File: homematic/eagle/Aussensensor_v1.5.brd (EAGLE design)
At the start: 56.2 x 29.4 mm, 44 parts, among them IC1 Atmega 328P, IC2 MAX1724, IC3 MAX44009, IC4 TSL256FN, IC5 BMP180, IC6 BME280, IC7 DS18B20, M1 CC1101_WIRELES_MODULE, T1 IRML6344

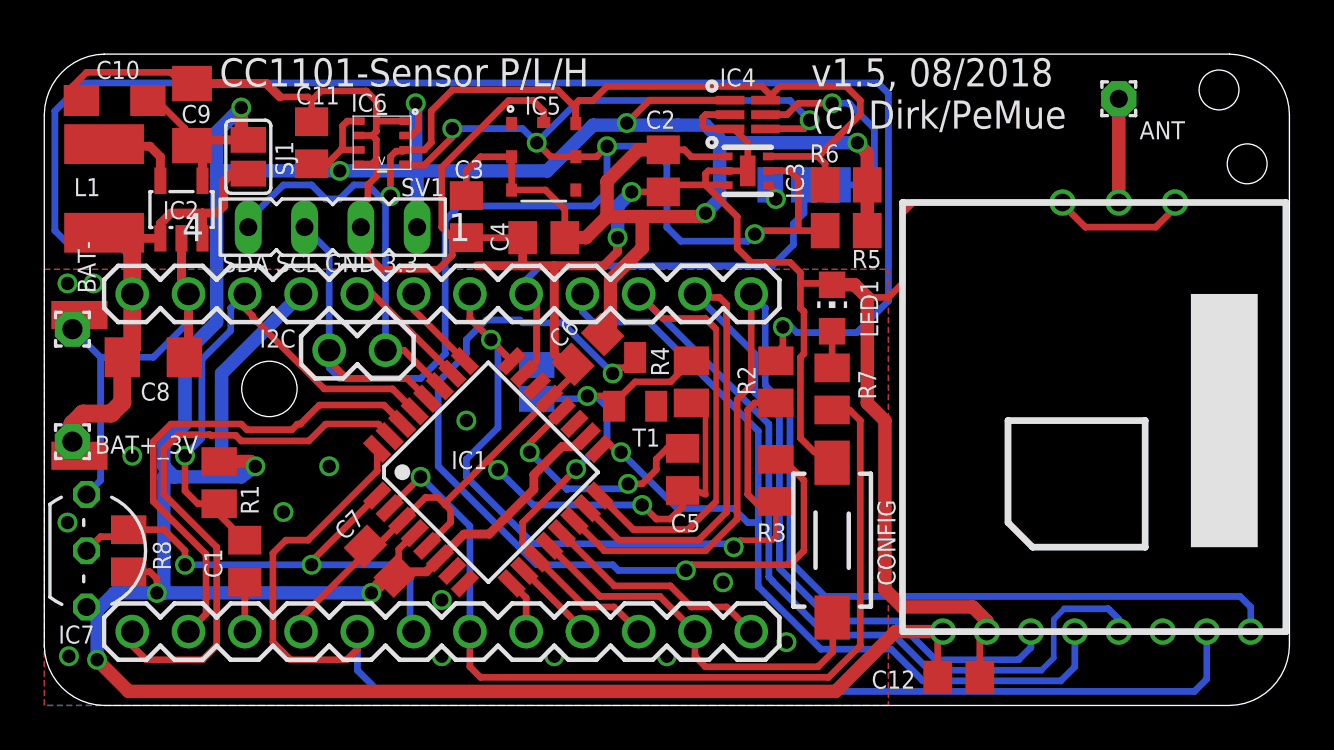
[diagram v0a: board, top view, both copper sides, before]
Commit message: - changes requested by Tom Major
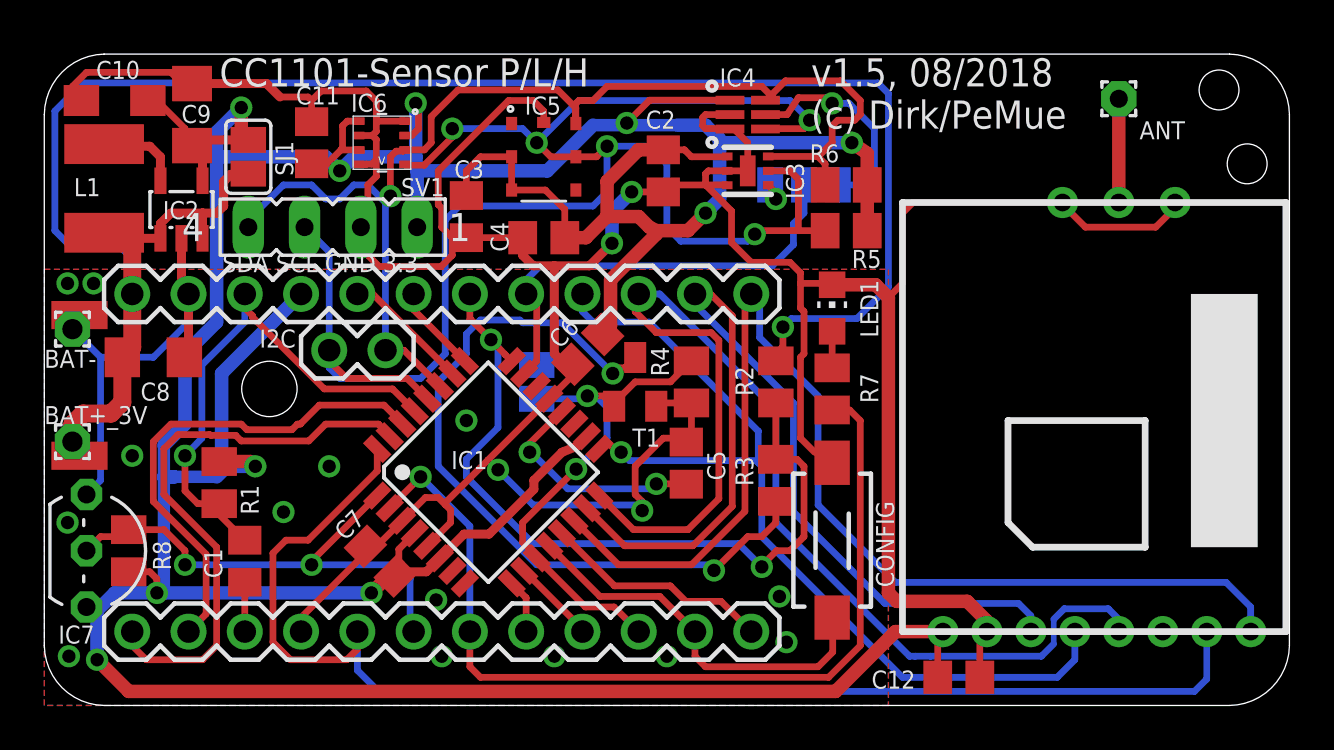
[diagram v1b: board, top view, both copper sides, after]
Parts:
- moved C5 0.33 mm to (29.0, 10.9), turned to 270 degrees
- turned R3 to 270 degrees
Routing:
- net GND: track 193.9 -> 189.1 mm
- net N$3: track 41.1 -> 36.9 mm
- net SCK: track 44.7 -> 41.8 mm
- net MOSI: track 46.4 -> 43.7 mm
- net D10: track 54.5 -> 52.8 mm
- net MISO: track 54.0 -> 52.6 mm
- net A1: track 34.6 -> 35.6 mm
- net U-BAT: track 88.2 -> 87.6 mm
- net +3.3V: track 212.8 -> 213.4 mm
- net SDA: track 54.7 -> 55.2 mm

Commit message: Changed compared to previous version: - all vias diameter 0.7, drill 0,4 mm - moved vias for buffer capacitor C3 and C11 - improved layout for C6 - R9 (pull up for CSN) added
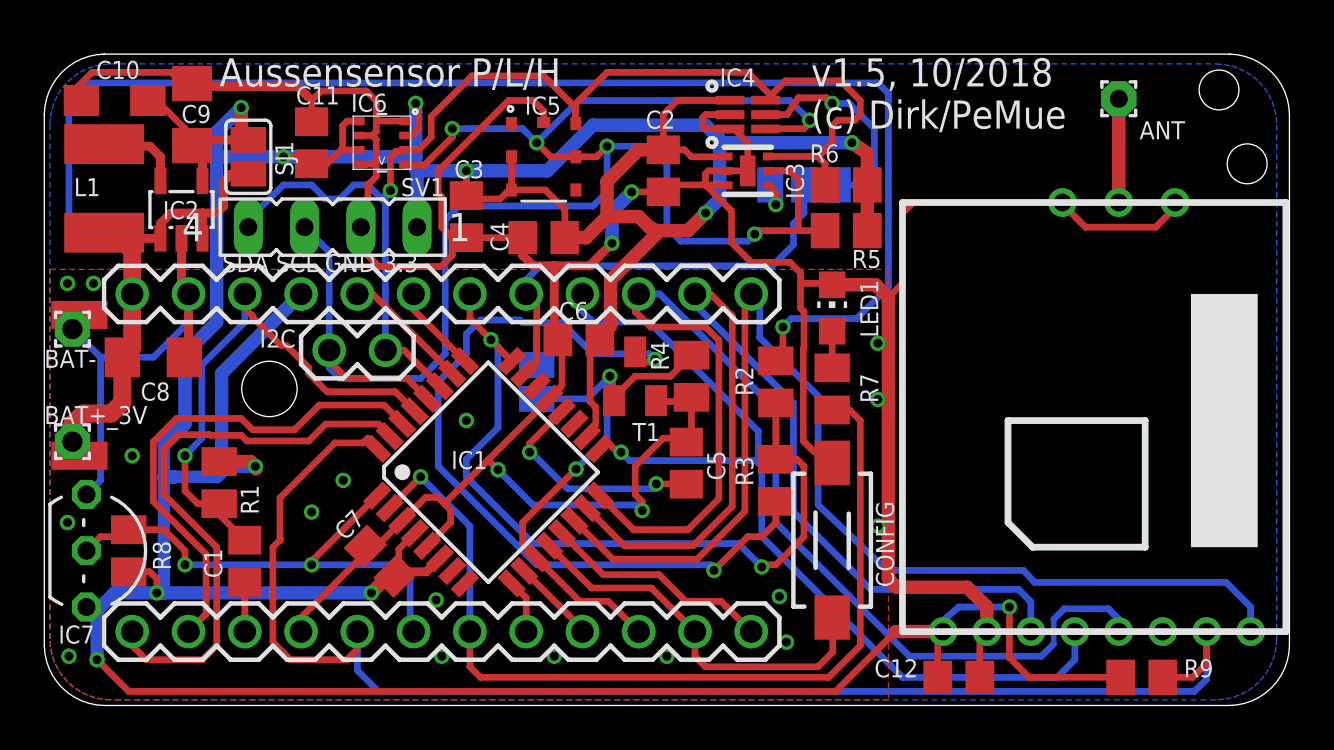
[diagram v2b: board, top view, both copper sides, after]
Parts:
- added R9: 100k, rcl:M0805
- moved C6 0.59 mm to (24.1, 16.5), turned to 0 degrees
- moved R4 0.25 mm to (29.2, 14.9)
- moved T1 0.25 mm to (26.7, 14.9)
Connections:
- net +3.3V: now also R9.2
- net D2: now also R9.1
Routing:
- net +3.3V: track 213.4 -> 222.0 mm, vias 10 -> 11
- net D2: track 59.2 -> 64.1 mm
- net D7: track 24.0 -> 25.9 mm
- net N$3: track 36.9 -> 38.5 mm
- net GND: track 189.1 -> 187.9 mm, vias 18 -> 21
- net SDA: track 55.2 -> 56.1 mm
- net U-BAT: track 87.6 -> 86.7 mm
- net INT_MAX: track 1.50 -> 2.01 mm
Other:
- board text added: "Aussensensor P/L/H"
- board text added: "v1.5, 10/2018 (c) Dirk/PeMue"
- board text removed: "CC1101-Sensor P/L/H"
- board text removed: "v1.5, 08/2018 (c) Dirk/PeMue"

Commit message: replaced 10k by 4k7 for DS18x20 in Aussensensor v1.4 and v1.5
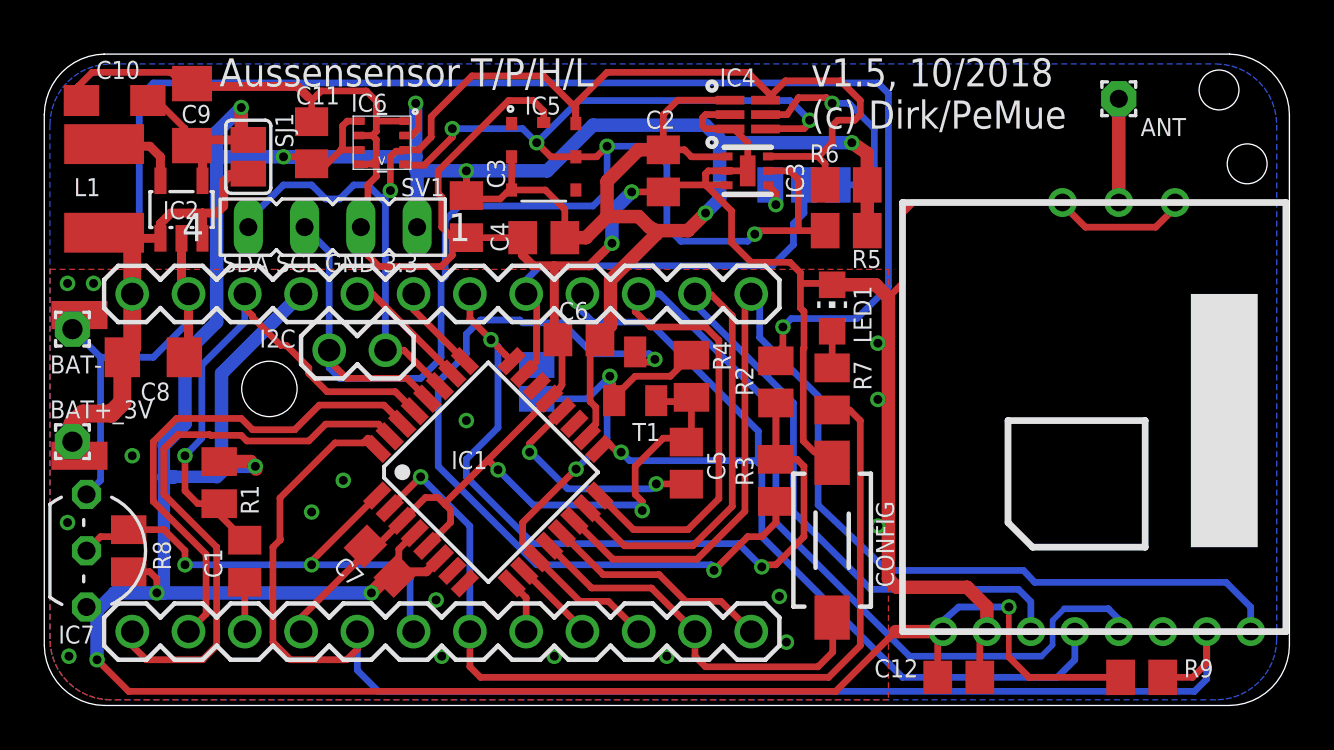
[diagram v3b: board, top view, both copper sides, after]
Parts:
- R8: value 10k -> 4k7
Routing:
- net U-BAT: track 86.7 -> 81.5 mm
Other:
- board text added: "Aussensensor T/P/H/L"
- board text removed: "Aussensensor P/L/H"

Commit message: replace Aussensensor v1.5 with a better readable schematic (no layout change)
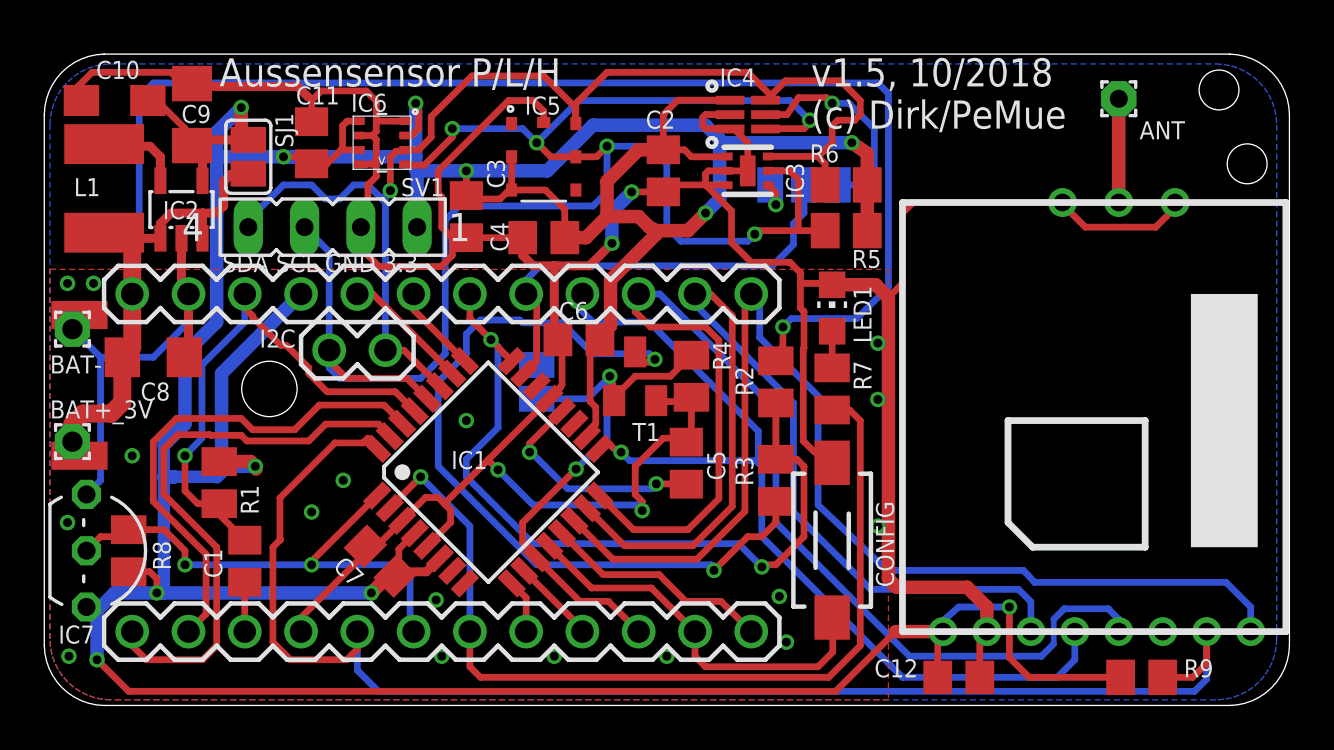
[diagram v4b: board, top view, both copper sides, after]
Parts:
- R2: value 8,2/22 -> 470/33/22
- R3: value 8,2 -> 100/10/22
- R4, R5, R6: value 4,7k -> 4.7k
- R7: value 1,5k -> 1.5k
- R8: value 4k7 -> 10k
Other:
- board text added: "Aussensensor P/L/H"
- board text removed: "Aussensensor T/P/H/L"

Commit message: update to previous version: - changed pull-up to 4k7 in Aussensensor_v1.5.sch and brd - added Aussensensor_v1.5_bom.xls
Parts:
- R8: value 10k -> 4k7
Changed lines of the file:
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@@
 <attribute name="VALUE" x="-1.397" y="9.525" size="1.27" layer="27" ratio="10" rot="R270"/>
 </element>
-<element name="R8" library="rcl" package="M0805" value="10k" x="3.81" y="6.985" smashed="yes" rot="R90">
+<element name="R8" library="rcl" package="M0805" value="4k7" x="3.81" y="6.985" smashed="yes" rot="R90">
 <attribute name="NAME" x="5.715" y="6.096" size="0.8128" layer="25" rot="R90"/>
 <attribute name="VALUE" x="6.096" y="5.969" size="1.27" layer="27" rot="R90"/>

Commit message: Changes to previous version: - updated R-divider for voltage measurement in Aussensensor_v1.5_bom.xls and the eagle files, printed PDF of schematic (Aussensensor_v1.5_sch.pdf)
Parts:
- R2: value 470/33/22 -> 470/33/10
- R3: value 100/10/22 -> 100/10/10
- T1: value IRML6344 -> IRML6344/SI2302
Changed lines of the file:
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@@
 <attribute name="NAME" x="38.354" y="5.334" size="0.8128" layer="25" rot="R90"/>
 </element>
-<element name="R2" library="rcl" package="M0805" value="470/33/22" x="33.02" y="14.605" smashed="yes" rot="R270">
+<element name="R2" library="rcl" package="M0805" value="470/33/10" x="33.02" y="14.605" smashed="yes" rot="R270">
 <attribute name="NAME" x="32.004" y="13.97" size="0.8128" layer="25" rot="R90"/>
 <attribute name="VALUE" x="30.734" y="15.621" size="1.27" layer="27" rot="R270"/>
 </element>
-<element name="R3" library="rcl" package="M0805" value="100/10/22" x="33.02" y="10.16" smashed="yes" rot="R270">
+<element name="R3" library="rcl" package="M0805" value="100/10/10" x="33.02" y="10.16" smashed="yes" rot="R270">
 <attribute name="NAME" x="32.004" y="9.906" size="0.8128" layer="25" rot="R90"/>
 <attribute name="VALUE" x="30.734" y="11.176" size="1.27" layer="27" rot="R270"/>
@@
 <attribute name="VALUE" x="4.775" y="29.305" size="1.016" layer="27" rot="R180"/>
 </element>
-<element name="T1" library="transistor-small-signal" package="SOT23" value="IRML6344" x="26.67" y="14.859" smashed="yes">
+<element name="T1" library="transistor-small-signal" package="SOT23" value="IRML6344/SI2302" x="26.67" y="14.859" smashed="yes">
 <attribute name="NAME" x="26.543" y="11.938" size="0.8128" layer="25"/>
 <attribute name="VALUE" x="24.765" y="11.684" size="1.27" layer="27"/>
